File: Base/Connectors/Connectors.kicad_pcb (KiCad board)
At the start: 2 copper layers, 80 x 50 mm, 18 parts, among them J1 Barrel_Jack_Switch, J2 AudioJack2_Ground, J3 AudioJack2_Ground, J4 RJ45_LED_Shielded, J5 USB_C_Receptacle_USB2.0_16P, Q1 40V

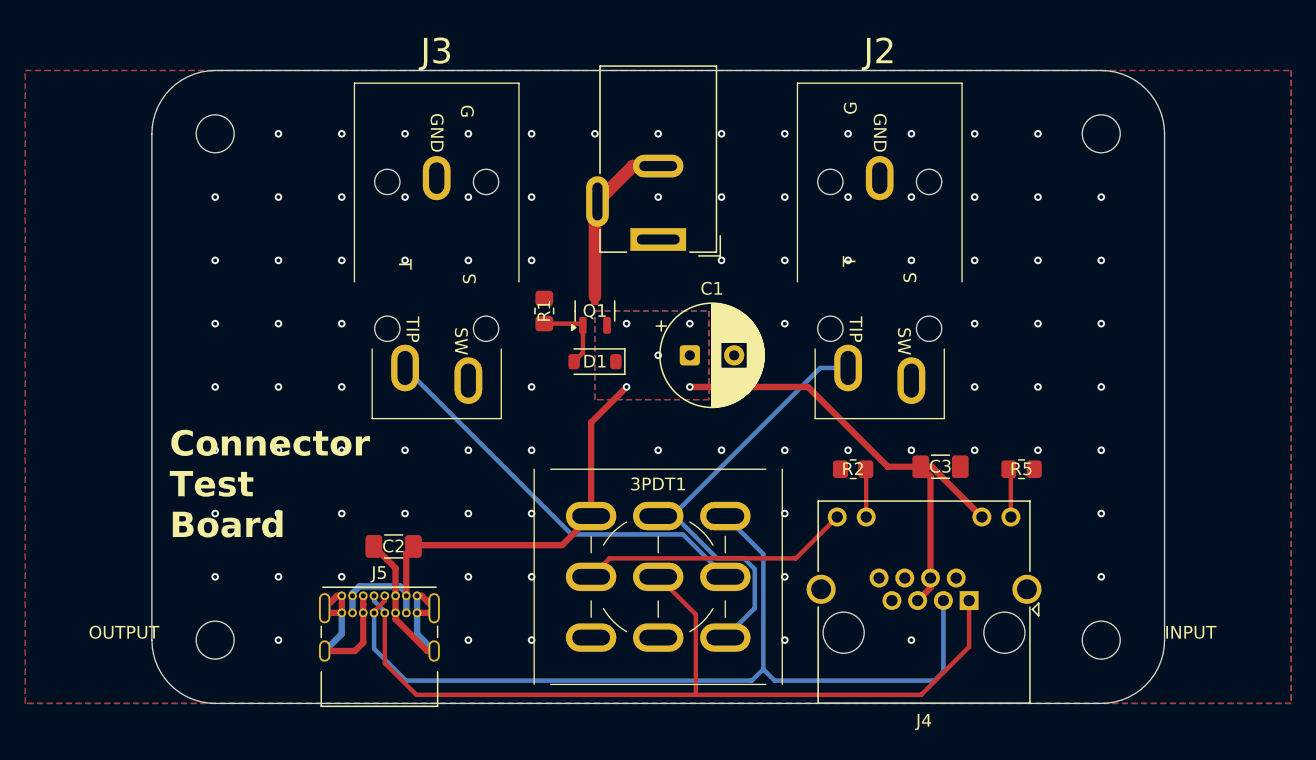
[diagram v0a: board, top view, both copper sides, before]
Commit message: Simplify the connector testing to just a USB-C connector
This is mainly to see what that would look like, particularly for the
base that now becomes really simple and small.

The effect connector ends up being crazy large just because of the old
pin header layout.  But the point of all this is that if it works out,
we'll dispense with the pin headers, and just use the USB-C connector
"natively".

So the effects board is just a temporary thing, and the base board is
where it's at.  If the base board works well, and I can stop soldering
stomp switches, I'll be good.

Signed-off-by: Linus Torvalds <torvalds@linux-foundation.org>
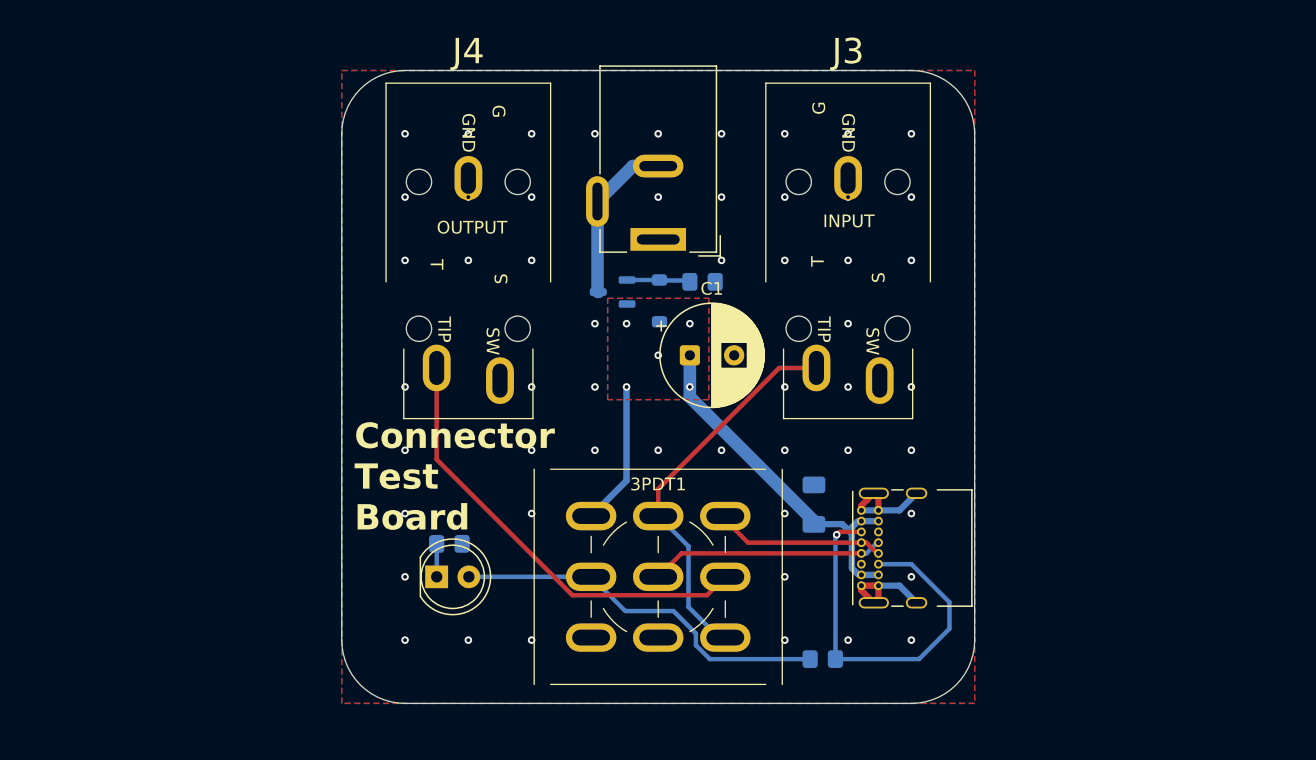
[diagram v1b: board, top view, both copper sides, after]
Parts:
- removed C3: 10uF, Capacitor_SMD:C_1206_3216Metric_Pad1.33x1.80mm_HandSolder
- removed H1, H2, H3, H4: MountingHole, MountingHole:MountingHole_3mm
- removed the J4 at (124.6, 116.9)
- removed R5: 2.2k, Resistor_SMD:R_0805_2012Metric_Pad1.20x1.40mm_HandSolder
- added D2: LED, LED_THT:LED_D5.0mm, F.Cu at (82.5, 115.0)
- added R3: 2k2, Resistor_SMD:R_0805_2012Metric_Pad1.20x1.40mm_HandSolder, B.Cu at (113.0, 121.5)
- C2, D1, Q1, R1: moved to B.Cu
- R2: value 2.2k -> 2k2; moved to B.Cu
- moved J2 41.1 mm to (116.0, 115.7), turned to 90 degrees
- moved C2 33.4 mm to (112.3, 109.3), turned to 90 degrees
- moved R2 32.4 mm to (83.5, 112.4)
- moved R1 12.7 mm to (103.5, 91.7), turned to 0 degrees
- moved D1 7.00 mm to (100.1, 93.2), turned to 90 degrees
- moved J3 2.50 mm to (115.0, 83.5)
- moved J4 2.50 mm to (85.0, 83.5)
- moved Q1 2.05 mm to (96.4, 92.5), turned to 180 degrees
- renumbered J5 to J2, J2 to J3, J3 to J4
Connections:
- J2 pad A5: GND -> unconnected-(J2-CC1-PadA5)
- J2 pad A8: GND -> Net-(J2-SBU1)
- J2 pad B5: GND -> unconnected-(J2-CC2-PadB5)
- J2 pad B8: GND -> Net-(J2-SBU1)
- R2 pad 1: Net-(J4-Pad11) -> GND
- R2 pad 2: GND -> Net-(D2-K)
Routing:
- net OUT^{RAW}: track 70.6 -> 13.5 mm
- net IN^{RAW}: track 68.7 -> 18.5 mm
- net VIN: track 77.0 -> 40.0 mm
- net Net-(J2-SBU1): track 0.00 -> 30.9 mm, vias 0 -> 1
- net GND: track 34.3 -> 16.4 mm, vias 88 -> 53
- net ACTIVE: track 21.4 -> 30.0 mm
- net IN^{CONN}: track 35.6 -> 30.7 mm
- net Net-(J4-Pad9): track 3.84 -> 0.00 mm
- net Net-(J4-Pad11): track 3.79 -> 0.00 mm
- net OUT^{CONN}: track 32.1 -> 35.1 mm
- net Net-(D2-K): track 0.00 -> 2.60 mm
- net Net-(D1-A): track 6.26 -> 5.02 mm
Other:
- board size 80 x 50 mm -> 50 x 50 mm
